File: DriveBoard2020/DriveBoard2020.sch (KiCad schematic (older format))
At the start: 30 parts

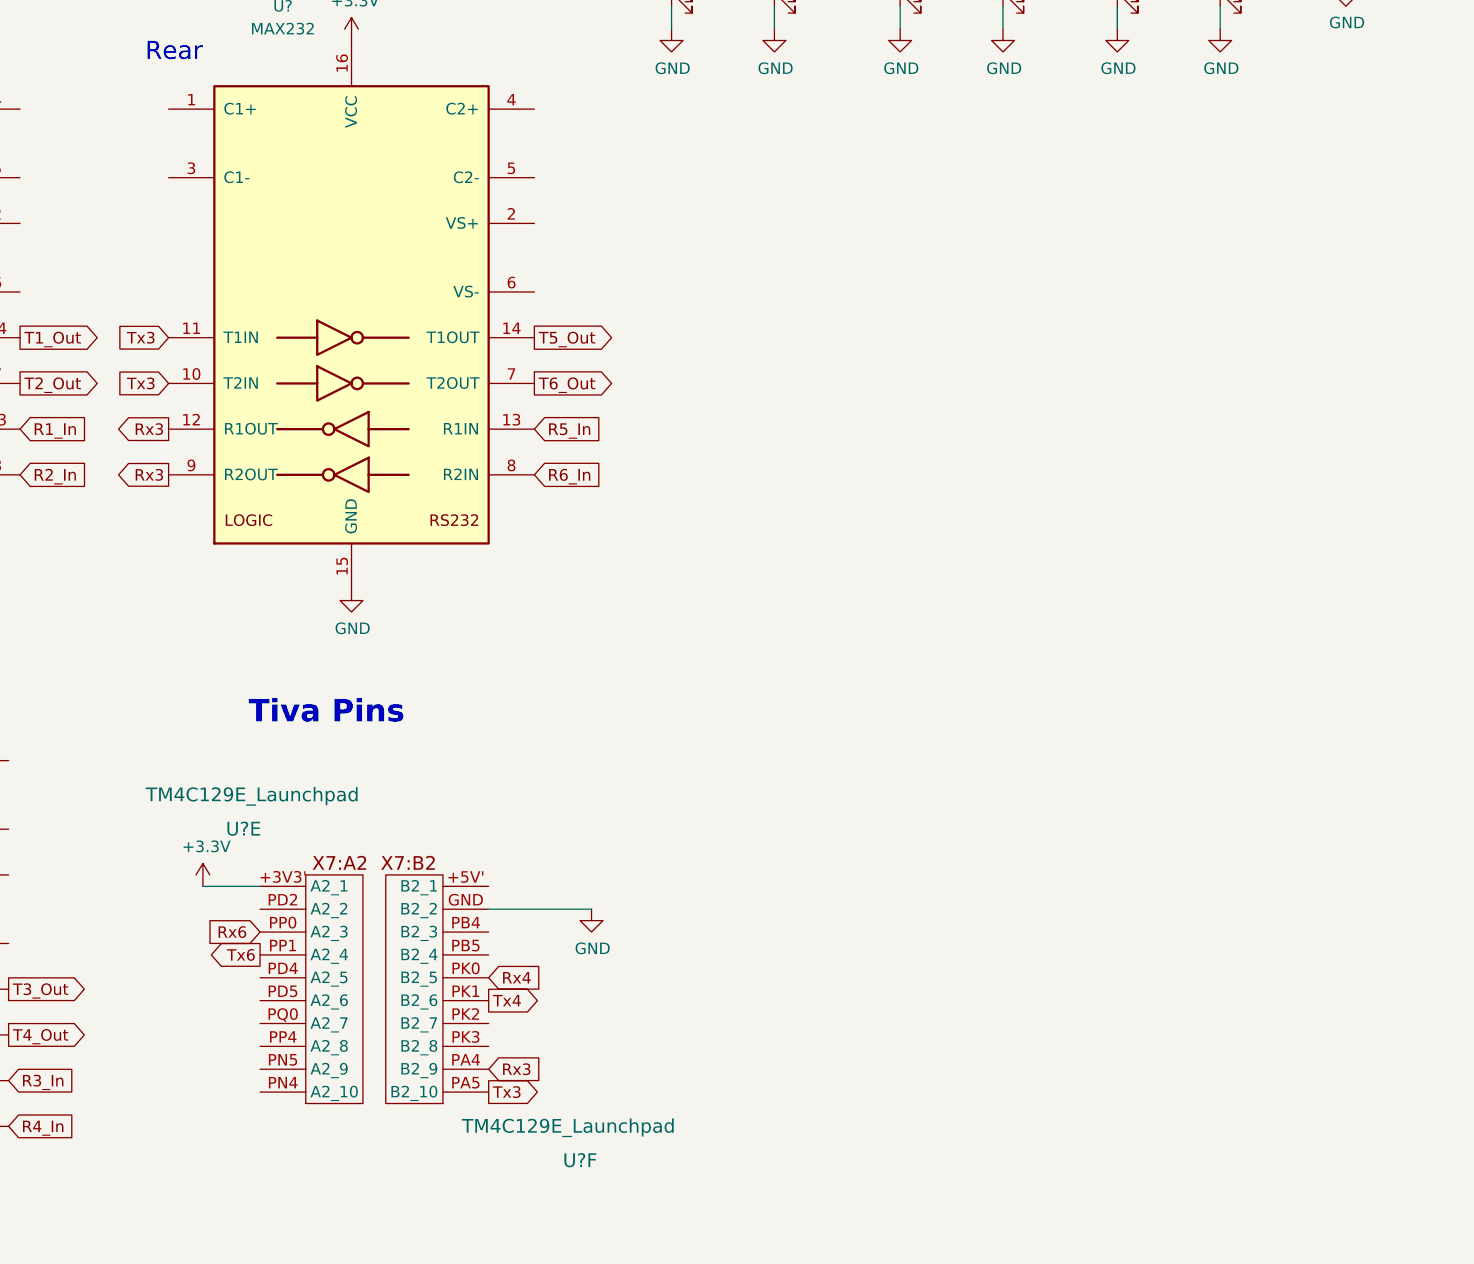
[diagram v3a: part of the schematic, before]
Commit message: Switches and buttons, forwarded to TIVA
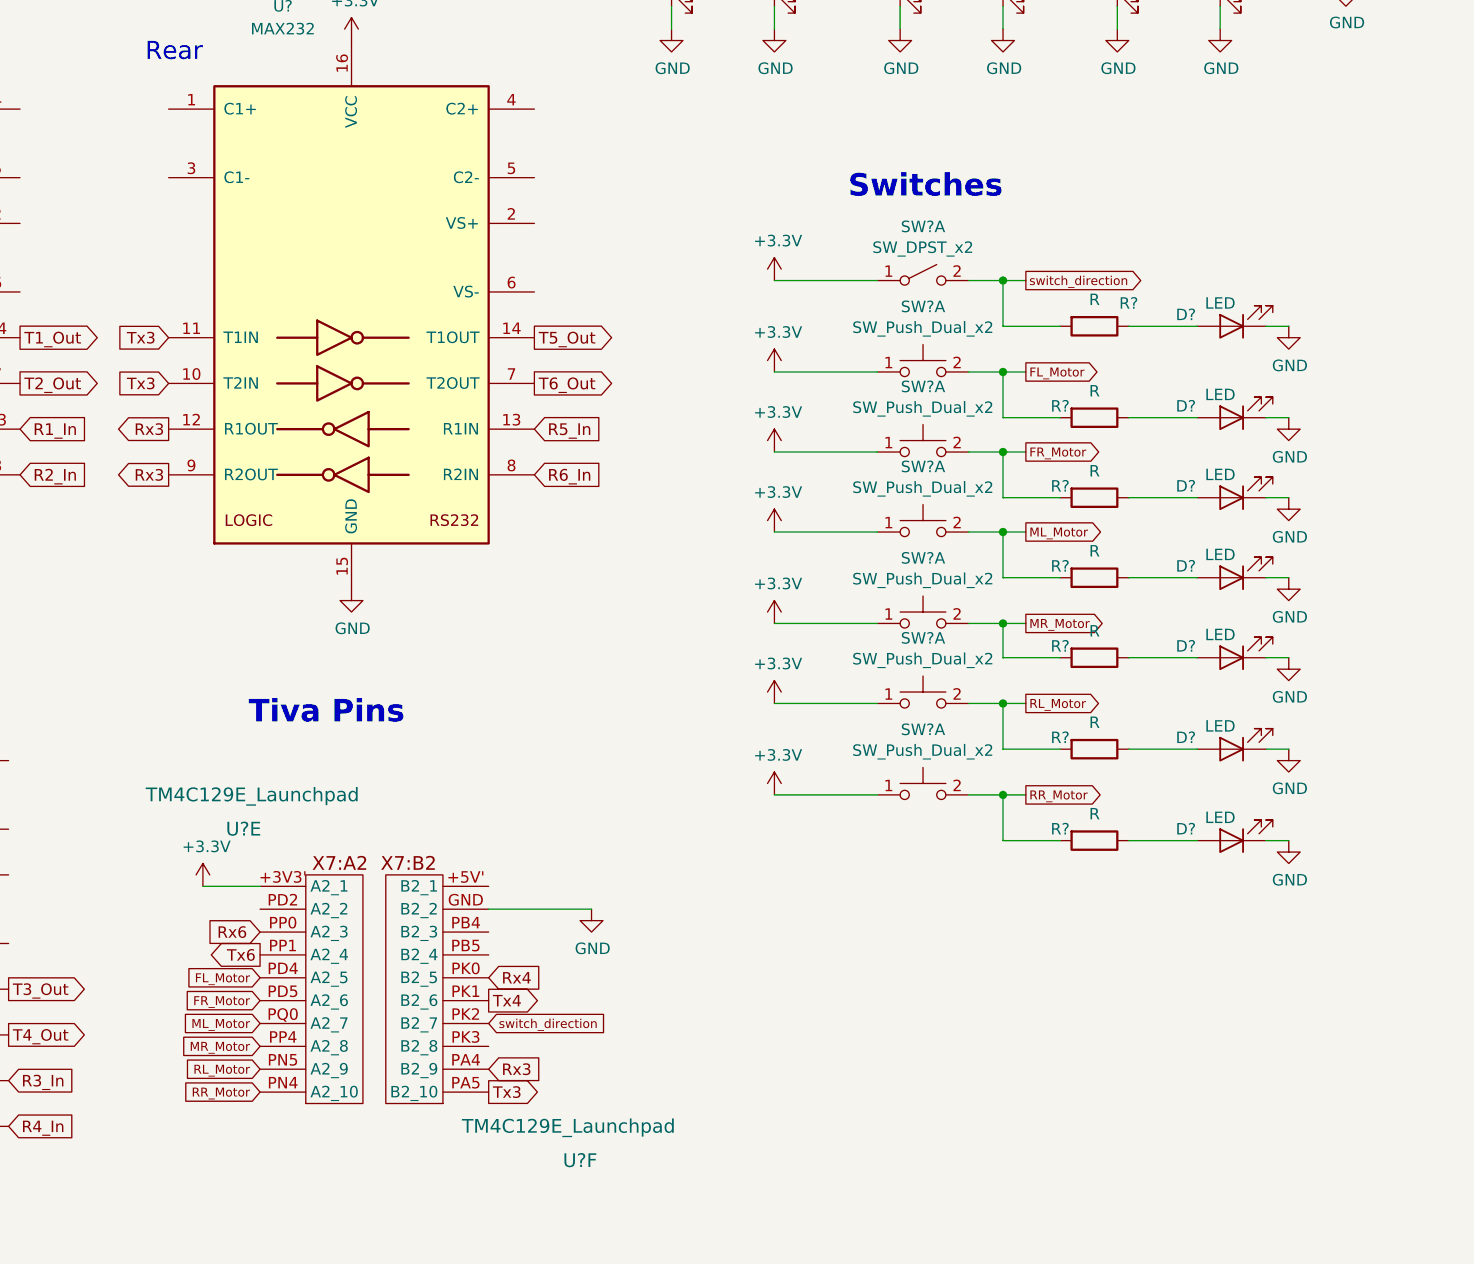
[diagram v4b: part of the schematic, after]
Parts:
- added D? (x7): LED, symbol Device:LED
- added R? (x7): R, symbol Device:R
- added SW?: SW_DPST_x2, symbol Switch:SW_DPST_x2
- added SW? (x6): SW_Push_Dual_x2, symbol Switch:SW_Push_Dual_x2
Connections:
- net +3V3: now also SW?.1 (A), SW?.1 (C), SW?.1 (C), SW?.1 (C), SW?.1 (C), SW?.1 (C), SW?.1 (C)
- net GND: now also D?.1 (K), D?.1 (K), D?.1 (K), D?.1 (K), D?.1 (K), D?.1 (K), D?.1 (K)
- net FL_Motor: now reaches U?.PD4 (A2_5)
- net FL_Motor: now also R?.2, SW?.2 (D)
- net FR_Motor: now reaches U?.PD5 (A2_6)
- net FR_Motor: now also R?.2, SW?.2 (D)
- net RR_Motor: now reaches U?.PN4 (A2_10)
- net RR_Motor: now also R?.2, SW?.2 (D)
- net RL_Motor: now reaches U?.PN5 (A2_9)
- net RL_Motor: now also R?.2, SW?.2 (D)
- net MR_Motor: now reaches U?.PP4 (A2_8)
- net MR_Motor: now also R?.2, SW?.2 (D)
- net ML_Motor: now reaches U?.PQ0 (A2_7)
- net ML_Motor: now also R?.2, SW?.2 (D)
- net switch_direction: now reaches U?.PK2 (B2_7)
- net switch_direction: now also R?.2, SW?.2 (B)
- new net: D?.2 (A), R?.1 (x7)
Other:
- note added: "Switches"
